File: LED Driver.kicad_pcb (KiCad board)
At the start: 2 copper layers, 18 x 15 mm, 8 parts, among them J1 CONN_01X02, J2 CONN_01X03, U1 AP5724

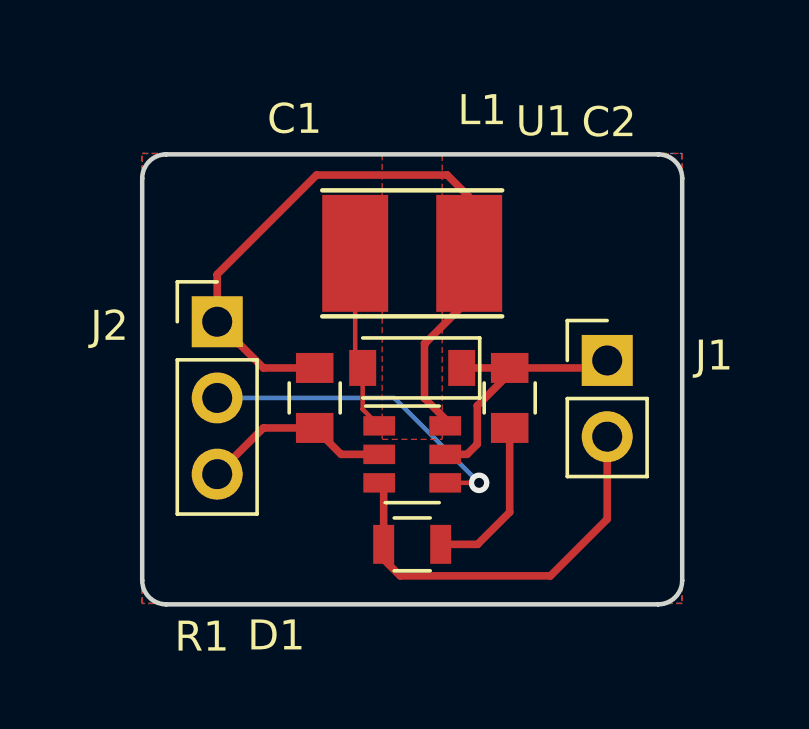
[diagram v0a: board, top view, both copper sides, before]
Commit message: Reworked layout to bring C1 closer to VCC input of AP5724
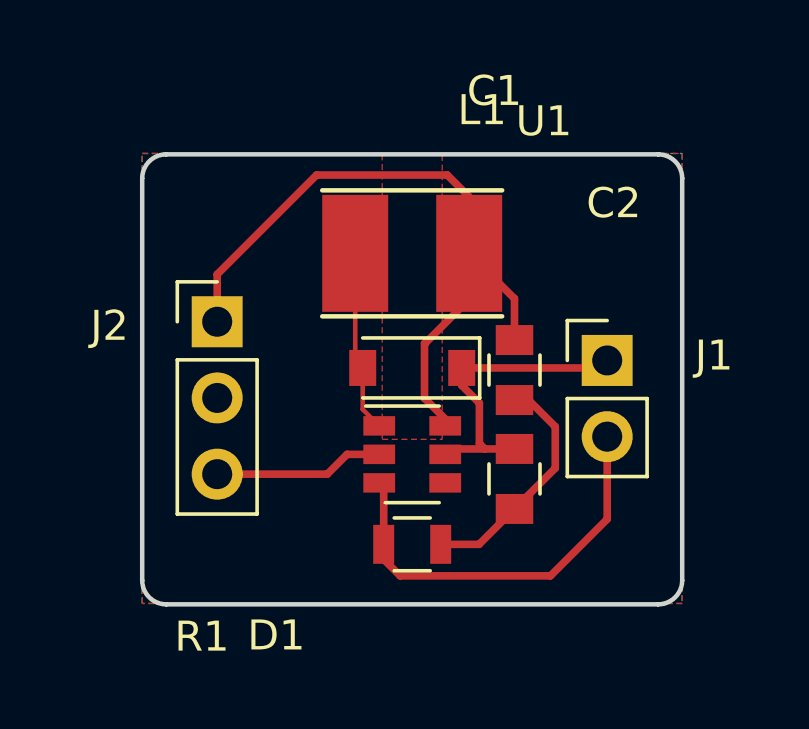
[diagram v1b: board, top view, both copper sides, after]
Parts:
- moved C1 6.72 mm to (112.4, 92.2)
- moved C2 2.70 mm to (112.4, 95.8)
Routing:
- net /EN: track 11.0 -> 0.00 mm, vias 1 -> 0
- net /LED_A: track 9.16 -> 11.1 mm
- net GND: track 12.0 -> 13.7 mm

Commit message: Finished updated layout
Moved things around to place C1 and C2 on right side of AP5724
Shrinked board to 15 x 15 mm
Adds solder bridge for EN pin (VCC or EN pin)
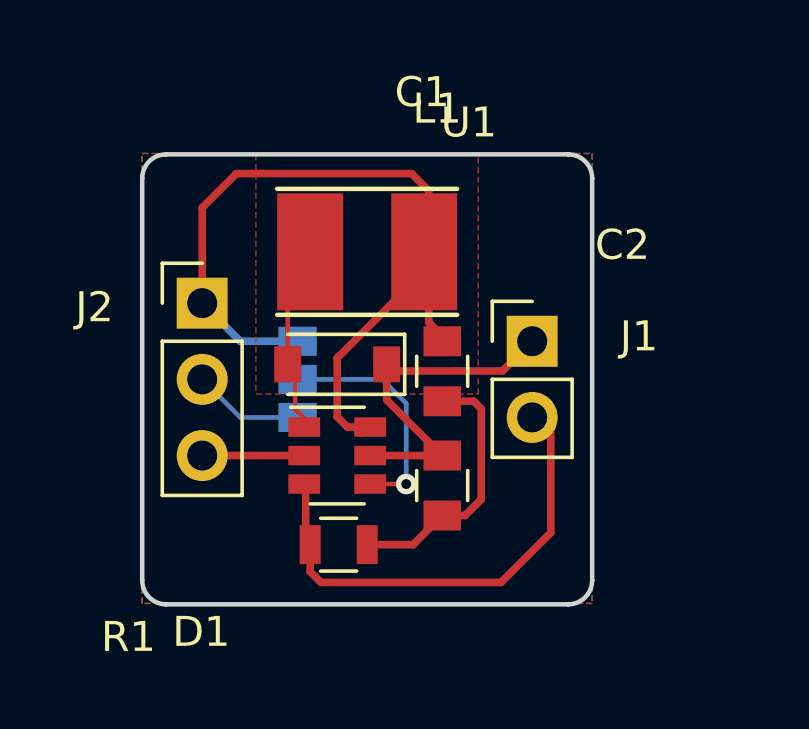
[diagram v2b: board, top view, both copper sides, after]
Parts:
- added J3: GS3, Connect:GS3, B.Cu at (105.2, 92.5)
- moved J1 2.58 mm to (113.0, 91.2)
- moved D1 2.50 mm to (106.5, 92.0)
- moved U1 2.50 mm to (106.5, 95.0)
- moved R1 2.45 mm to (106.5, 98.0)
- moved C2 2.42 mm to (110.0, 96.0)
- moved C1 2.41 mm to (110.0, 92.2)
- moved L1 1.50 mm to (107.5, 88.2)
- moved J2 0.80 mm to (102.0, 90.0)
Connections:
- J2 pad 2: /EN -> /EN_CONN
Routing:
- net +3V3: track 24.5 -> 34.8 mm
- net /EN: track 0.00 -> 7.84 mm, vias 0 -> 1
- net /EN_CONN: track 0.00 -> 3.71 mm
- net /LED_K: track 13.8 -> 15.5 mm
- net GND: track 13.7 -> 12.5 mm
- net /LED_A: track 11.1 -> 11.7 mm
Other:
- board size 18 x 15 mm -> 15 x 15 mm

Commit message: Replaces AP5824 with NCP5006, removed unnecessary OV track, minor cleanup
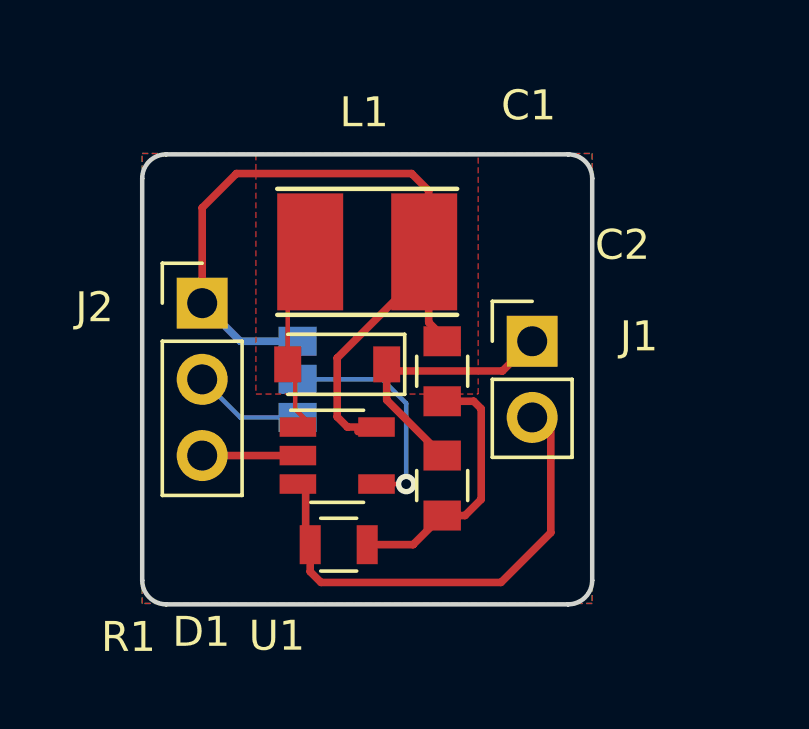
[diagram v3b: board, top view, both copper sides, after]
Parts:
- C1: value 1uF -> 4.7uF
- D1: value SDM20U40 -> MBR0530
- R1: value 2.55 -> 5.1
- U1: value AP5724 -> NCP5006; footprint TO_SOT_Packages_SMD:SOT-23-6 -> TO_SOT_Packages_SMD:TSOT-23-5
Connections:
- U1 pad 5: /LED_A -> +3V3
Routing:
- net /LED_A: track 11.7 -> 9.33 mm
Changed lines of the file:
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@@
 (kicad_pcb (version 4) (host pcbnew 4.0.6)
   (general
-    (links 17)
+    (links 16)
     (no_connects 0)
     (area 99.924999 84.924999 115.075001 100.075001)
     (thickness 1.6)
     (drawings 8)
-    (tracks 54)
+    (tracks 53)
     (zones 0)
     (modules 9)
@@
     (44 Edge.Cuts user)
     (45 Margin user)
-    (46 B.CrtYd user)
+    (46 B.CrtYd user hide)
     (47 F.CrtYd user)
-    (48 B.Fab user)
-    (49 F.Fab user)
+    (48 B.Fab user hide)
+    (49 F.Fab user hide)
   )
   (setup
@@
     (add_net GND)
   )
-  (module TO_SOT_Packages_SMD:SOT-23-6 locked (layer F.Cu)
-    (at 106.5 95.04)
-    (descr "6-pin SOT-23 package")
-    (tags SOT-23-6)
-    (attr smd)
-    (fp_text reference U1 (at 4.39 -11.1) (layer F.SilkS)
-      (effects (font (size 1 1) (thickness 0.15)))
-    )
-    (fp_text value AP5724 (at -0.11 -4.64) (layer F.Fab)
-      (effects (font (size 1 1) (thickness 0.15)))
-    )
-    (fp_text user %R (at 0 -0.01 90) (layer F.Fab) hide
-      (effects (font (size 0.5 0.5) (thickness 0.075)))
-    )
-    (fp_line (start -0.9 1.61) (end 0.9 1.61) (layer F.SilkS) (width 0.12))
-    (fp_line (start 0.9 -1.61) (end -1.55 -1.61) (layer F.SilkS) (width 0.12))
-    (fp_line (start 1.9 -1.8) (end -1.9 -1.8) (layer F.CrtYd) (width 0.05))
-    (fp_line (start 1.9 1.8) (end 1.9 -1.8) (layer F.CrtYd) (width 0.05))
-    (fp_line (start -1.9 1.8) (end 1.9 1.8) (layer F.CrtYd) (width 0.05))
-    (fp_line (start -1.9 -1.8) (end -1.9 1.8) (layer F.CrtYd) (width 0.05))
-    (fp_line (start -0.9 -0.9) (end -0.25 -1.55) (layer F.Fab) (width 0.1))
-    (fp_line (start 0.9 -1.55) (end -0.25 -1.55) (layer F.Fab) (width 0.1))
-    (fp_line (start -0.9 -0.9) (end -0.9 1.55) (layer F.Fab) (width 0.1))
-    (fp_line (start 0.9 1.55) (end -0.9 1.55) (layer F.Fab) (width 0.1))
-    (fp_line (start 0.9 -1.55) (end 0.9 1.55) (layer F.Fab) (width 0.1))
-    (pad 1 smd rect (at -1.1 -0.95) (size 1.06 0.65) (layers F.Cu F.Paste F.Mask)
-      (net 4 "Net-(D1-Pad2)"))
-    (pad 2 smd rect (at -1.1 0) (size 1.06 0.65) (layers F.Cu F.Paste F.Mask)
-      (net 2 GND))
-    (pad 3 smd rect (at -1.1 0.95) (size 1.06 0.65) (layers F.Cu F.Paste F.Mask)
-      (net 5 /LED_K))
-    (pad 4 smd rect (at 1.1 0.95) (size 1.06 0.65) (layers F.Cu F.Paste F.Mask)
-      (net 6 /EN))
-    (pad 6 smd rect (at 1.1 -0.95) (size 1.06 0.65) (layers F.Cu F.Paste F.Mask)
-      (net 1 +3V3))
-    (pad 5 smd rect (at 1.1 0) (size 1.06 0.65) (layers F.Cu F.Paste F.Mask)
-      (net 3 /LED_A))
-    (model ${KISYS3DMOD}/TO_SOT_Packages_SMD.3dshapes/SOT-23-6.wrl
-      (at (xyz 0 0 0))
-      (scale (xyz 1 1 1))
-      (rotate (xyz 0 0 0))
-    )
-  )
   (module Capacitors_SMD:C_0805 (layer F.Cu)
     (at 110 96.04 270)
@@
     (tags "capacitor 0805")
     (attr smd)
-    (fp_text reference C1 (at -9.3 0.67 360) (layer F.SilkS)
-      (effects (font (size 1 1) (thickness 0.15)))
-    )
-    (fp_text value 1uF (at 0 1.75 270) (layer F.Fab)
+    (fp_text reference C1 (at -8.86 -2.88 360) (layer F.SilkS)
+      (effects (font (size 1 1) (thickness 0.15)))
+    )
+    (fp_text value 4.7uF (at 0 1.75 270) (layer F.Fab)
       (effects (font (size 1 1) (thickness 0.15)))
     )
@@
     (tags "inductor taiyo-yuden nr smd")
     (attr smd)
-    (fp_text reference L1 (at -2.33 4.77 180) (layer F.SilkS)
+    (fp_text reference L1 (at 0.1 4.65 180) (layer F.SilkS)
       (effects (font (size 1 1) (thickness 0.15)))
     )
@@
       (effects (font (size 1 1) (thickness 0.15)))
     )
-    (fp_text value 2.55 (at 0 1.75) (layer F.Fab)
+    (fp_text value 5.1 (at 0 1.75) (layer F.Fab)
       (effects (font (size 1 1) (thickness 0.15)))
     )
@@
       (effects (font (size 1 1) (thickness 0.15)))
     )
-    (fp_text value SDM20U40 (at 0 2.1 180) (layer F.Fab)
+    (fp_text value MBR0530 (at 0 2.1 180) (layer F.Fab)
       (effects (font (size 1 1) (thickness 0.15)))
     )
@@
     (pad 3 smd rect (at 0 -1.27 180) (size 1.27 0.97) (layers B.Cu B.Paste B.Mask)
       (net 7 /EN_CONN))
+  )
+  (module TO_SOT_Packages_SMD:TSOT-23-5 locked (layer F.Cu)
+    (at 106.5 95.04)
+    (descr "5-pin TSOT23 package, http://cds.linear.com/docs/en/packaging/SOT_5_05-08-1635.pdf")
+    (tags TSOT-23-5)
+    (attr smd)
+    (fp_text reference U1 (at -2.01 6.01) (layer F.SilkS)
+      (effects (font (size 1 1) (thickness 0.15)))
+    )
+    (fp_text value NCP5006 (at 0 2.5) (layer F.Fab)
+      (effects (font (size 1 1) (thickness 0.15)))
+    )
+    (fp_text user %R (at 0 0 90) (layer F.Fab)
+      (effects (font (size 0.5 0.5) (thickness 0.075)))
+    )
+    (fp_line (start -0.88 1.56) (end 0.88 1.56) (layer F.SilkS) (width 0.12))
+    (fp_line (start 0.88 -1.51) (end -1.55 -1.51) (layer F.SilkS) (width 0.12))
+    (fp_line (start -0.88 -1) (end -0.43 -1.45) (layer F.Fab) (width 0.1))
+    (fp_line (start 0.88 -1.45) (end -0.43 -1.45) (layer F.Fab) (width 0.1))
+    (fp_line (start -0.88 -1) (end -0.88 1.45) (layer F.Fab) (width 0.1))
+    (fp_line (start 0.88 1.45) (end -0.88 1.45) (layer F.Fab) (width 0.1))
+    (fp_line (start 0.88 -1.45) (end 0.88 1.45) (layer F.Fab) (width 0.1))
+    (fp_line (start -2.17 -1.7) (end 2.17 -1.7) (layer F.CrtYd) (width 0.05))
+    (fp_line (start -2.17 -1.7) (end -2.17 1.7) (layer F.CrtYd) (width 0.05))
+    (fp_line (start 2.17 1.7) (end 2.17 -1.7) (layer F.CrtYd) (width 0.05))
+    (fp_line (start 2.17 1.7) (end -2.17 1.7) (layer F.CrtYd) (width 0.05))
+    (pad 1 smd rect (at -1.31 -0.95) (size 1.22 0.65) (layers F.Cu F.Paste F.Mask)
+      (net 4 "Net-(D1-Pad2)"))
+    (pad 2 smd rect (at -1.31 0) (size 1.22 0.65) (layers F.Cu F.Paste F.Mask)
+      (net 2 GND))
+    (pad 3 smd rect (at -1.31 0.95) (size 1.22 0.65) (layers F.Cu F.Paste F.Mask)
+      (net 5 /LED_K))
+    (pad 4 smd rect (at 1.31 0.95) (size 1.22 0.65) (layers F.Cu F.Paste F.Mask)
+      (net 6 /EN))
+    (pad 5 smd rect (at 1.31 -0.95) (size 1.22 0.65) (layers F.Cu F.Paste F.Mask)
+      (net 1 +3V3))
+    (model ${KISYS3DMOD}/TO_SOT_Packages_SMD.3dshapes/TSOT-23-5.wrl
+      (at (xyz 0 0 0))
+      (scale (xyz 1 1 1))
+      (rotate (xyz 0 0 0))
+    )
   )
   (gr_arc (start 114.2 99.2) (end 115 99.2) (angle 90) (layer Edge.Cuts) (width 0.15))
@@
   (segment (start 108.37 92.22) (end 112.01 92.22) (width 0.254) (layer F.Cu) (net 3))
   (segment (start 112.01 92.22) (end 113 91.23) (width 0.254) (layer F.Cu) (net 3))
-  (segment (start 107.6 95.04) (end 110 95.04) (width 0.254) (layer F.Cu) (net 3))
   (segment (start 110.32 95.19) (end 110.44 95.31) (width 0.254) (layer F.Cu) (net 3))
   (segment (start 105.65 94.05) (end 105.1 93.5) (width 0.1524) (layer F.Cu) (net 4))

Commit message: Adds explicit VOUT net, moves it "Power" class
Removed unnecessary tracks, overall cleanup
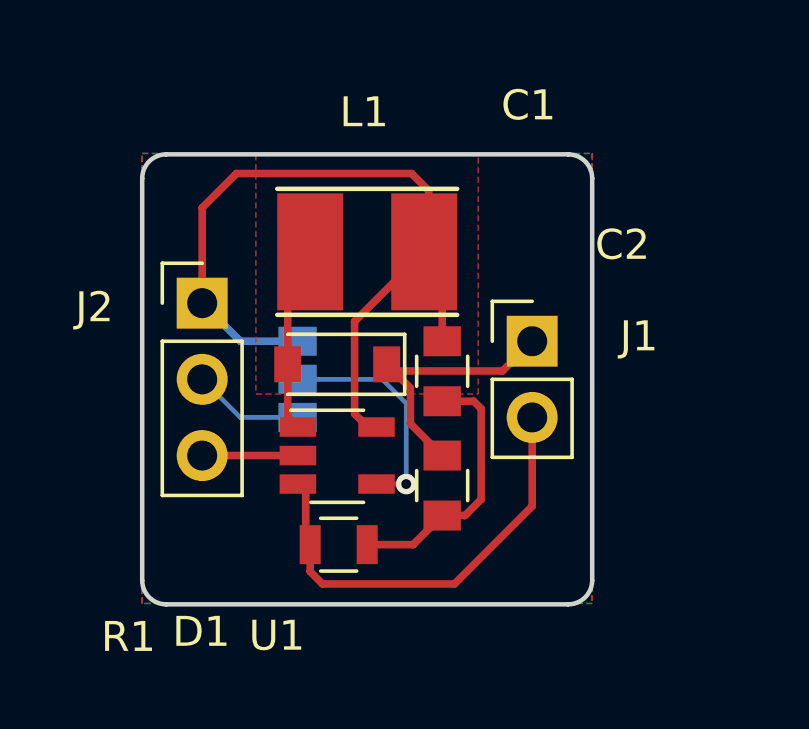
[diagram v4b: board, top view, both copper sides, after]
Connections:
- net Net-(D1-Pad2) renamed /VOUT
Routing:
- net +3V3: track 34.8 -> 27.2 mm
- net /LED_K: track 15.5 -> 14.4 mm
